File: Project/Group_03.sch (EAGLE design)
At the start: 18 parts, among them J1 POWER_JACKPTH_LOCK, U1 +12v, U3 TCA9546APW

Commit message: Add last comments + layout editing
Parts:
- added J2, J3, J4, J5: (no value), SparkFun-Connectors:CONN_02
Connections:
- net I2C_SCL_0: now also J2.2
- net I2C_SCL_1: now also J3.2
- net I2C_SCL_2: now also J4.2
- net I2C_SCL_3: now also J5.2
- net I2C_SDA_0: now also J2.1
- net I2C_SDA_1: now also J3.1
- net I2C_SDA_2: now also J4.1
- net I2C_SDA_3: now also J5.1
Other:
- note added: "4-Channel I2C"
- note added: "Analog Temeprature Sensor"
- note added: "Light Sensor"
- note added: "Power"
- note added: "The I2C expander is used to connect several BME280 sensors outside the PCB through these connectors."
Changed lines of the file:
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@@
 <part name="GND5" library="SparkFun-PowerSymbols" deviceset="GND" device=""/>
 <part name="SUPPLY7" library="SparkFun-PowerSymbols" deviceset="5V" device=""/>
+<part name="J2" library="SparkFun-Connectors" deviceset="CONN_02" device=""/>
+<part name="J3" library="SparkFun-Connectors" deviceset="CONN_02" device=""/>
+<part name="J4" library="SparkFun-Connectors" deviceset="CONN_02" device=""/>
+<part name="J5" library="SparkFun-Connectors" deviceset="CONN_02" device=""/>
 </parts>
 <sheets>
@@
 <wire x1="132.08" y1="175.26" x2="271.78" y2="175.26" width="0.1524" layer="97"/>
 <wire x1="271.78" y1="175.26" x2="271.78" y2="101.6" width="0.1524" layer="97"/>
-<wire x1="271.78" y1="101.6" x2="132.08" y2="101.6" width="0.1524" layer="97"/>
+<wire x1="271.78" y1="101.6" x2="220.98" y2="101.6" width="0.1524" layer="97"/>
+<wire x1="220.98" y1="101.6" x2="132.08" y2="101.6" width="0.1524" layer="97"/>
 <wire x1="132.08" y1="101.6" x2="132.08" y2="134.62" width="0.1524" layer="97"/>
+<wire x1="271.78" y1="22.86" x2="271.78" y2="86.36" width="0.1524" layer="97"/>
+<text x="231.14" y="88.9" size="1.778" layer="97">The I2C expander is used to
+connect several BME280
+sensors outside the PCB
+through these connectors.</text>
+<wire x1="271.78" y1="86.36" x2="271.78" y2="101.6" width="0.1524" layer="97"/>
+<wire x1="220.98" y1="101.6" x2="220.98" y2="86.36" width="0.1524" layer="97"/>
+<wire x1="220.98" y1="86.36" x2="220.98" y2="22.86" width="0.1524" layer="97"/>
+<wire x1="220.98" y1="22.86" x2="271.78" y2="22.86" width="0.1524" layer="97"/>
+<wire x1="220.98" y1="86.36" x2="271.78" y2="86.36" width="0.1524" layer="97"/>
+<text x="30.48" y="60.96" size="1.778" layer="97">Analog Temeprature
+Sensor</text>
+<text x="38.1" y="73.66" size="1.778" layer="97">Light Sensor</text>
+<text x="60.96" y="139.7" size="1.778" layer="97">Power</text>
+<text x="167.64" y="170.18" size="1.778" layer="97">4-Channel I2C</text>
 </plain>
 <instances>
@@
 <instance part="SUPPLY7" gate="G$1" x="149.86" y="162.56" smashed="yes">
 <attribute name="VALUE" x="149.86" y="165.354" size="1.778" layer="96" align="bottom-center"/>
+</instance>
+<instance part="J2" gate="G$1" x="236.22" y="76.2" smashed="yes">
+<attribute name="VALUE" x="233.68" y="71.374" size="1.778" layer="96" font="vector"/>
+<attribute name="NAME" x="233.68" y="81.788" size="1.778" layer="95" font="vector"/>
+</instance>
+<instance part="J3" gate="G$1" x="236.22" y="60.96" smashed="yes">
+<attribute name="VALUE" x="233.68" y="56.134" size="1.778" layer="96" font="vector"/>
+<attribute name="NAME" x="233.68" y="66.548" size="1.778" layer="95" font="vector"/>
+</instance>
+<instance part="J4" gate="G$1" x="236.22" y="45.72" smashed="yes">
+<attribute name="VALUE" x="233.68" y="40.894" size="1.778" layer="96" font="vector"/>
+<attribute name="NAME" x="233.68" y="51.308" size="1.778" layer="95" font="vector"/>
+</instance>
+<instance part="J5" gate="G$1" x="236.22" y="30.48" smashed="yes">
+<attribute name="VALUE" x="233.68" y="25.654" size="1.778" layer="96" font="vector"/>
+<attribute name="NAME" x="233.68" y="36.068" size="1.778" layer="95" font="vector"/>
 </instance>
 </instances>
@@
 <label x="185.42" y="147.32" size="1.778" layer="95"/>
 </segment>
+<segment>
+<pinref part="J2" gate="G$1" pin="2"/>
+<wire x1="243.84" y1="78.74" x2="254" y2="78.74" width="0.1524" layer="91"/>
+<label x="246.38" y="78.74" size="1.778" layer="95"/>
+</segment>
 </net>
 <net name="I2C_SDA_0" class="0">
@@
 <label x="185.42" y="144.78" size="1.778" layer="95"/>
 </segment>
+<segment>
+<pinref part="J2" gate="G$1" pin="1"/>
+<wire x1="243.84" y1="76.2" x2="254" y2="76.2" width="0.1524" layer="91"/>
+<label x="246.38" y="76.2" size="1.778" layer="95"/>
+</segment>
 </net>
 <net name="I2C_SCL_1" class="0">
@@
 <label x="185.42" y="137.16" size="1.778" layer="95"/>
 </segment>
+<segment>
+<pinref part="J3" gate="G$1" pin="2"/>
+<wire x1="243.84" y1="63.5" x2="254" y2="63.5" width="0.1524" layer="91"/>
+<label x="246.38" y="63.5" size="1.778" layer="95"/>
+</segment>
 </net>
 <net name="I2C_SDA_1" class="0">
@@
 <label x="185.42" y="134.62" size="1.778" layer="95"/>
 </segment>
+<segment>
+<pinref part="J3" gate="G$1" pin="1"/>
+<wire x1="243.84" y1="60.96" x2="254" y2="60.96" width="0.1524" layer="91"/>
+<label x="246.38" y="60.96" size="1.778" layer="95"/>
+</segment>
 </net>
 <net name="I2C_SCL_2" class="0">
@@
 <label x="185.42" y="127" size="1.778" layer="95"/>
 </segment>
+<segment>
+<pinref part="J4" gate="G$1" pin="2"/>
+<wire x1="243.84" y1="48.26" x2="254" y2="48.26" width="0.1524" layer="91"/>
+<label x="246.38" y="48.26" size="1.778" layer="95"/>
+</segment>
 </net>
 <net name="I2C_SDA_2" class="0">
@@
 <label x="185.42" y="124.46" size="1.778" layer="95"/>
 </segment>
+<segment>
+<pinref part="J4" gate="G$1" pin="1"/>
+<wire x1="243.84" y1="45.72" x2="254" y2="45.72" width="0.1524" layer="91"/>
+<label x="246.38" y="45.72" size="1.778" layer="95"/>
+</segment>
 </net>
 <net name="I2C_SCL_3" class="0">
@@
 <label x="185.42" y="114.3" size="1.778" layer="95"/>
 </segment>
+<segment>
+<pinref part="J5" gate="G$1" pin="2"/>
+<wire x1="243.84" y1="33.02" x2="254" y2="33.02" width="0.1524" layer="91"/>
+<label x="246.38" y="33.02" size="1.778" layer="95"/>
+</segment>
 </net>
 <net name="I2C_SDA_3" class="0">
@@
 <wire x1="264.16" y1="111.76" x2="264.16" y2="119.38" width="0.1524" layer="91"/>
 <label x="185.42" y="111.76" size="1.778" layer="95"/>
+</segment>
+<segment>
+<pinref part="J5" gate="G$1" pin="1"/>
+<wire x1="243.84" y1="30.48" x2="254" y2="30.48" width="0.1524" layer="91"/>
+<label x="246.38" y="30.48" size="1.778" layer="95"/>
 </segment>
 </net>
@@
 </schematic>
 </drawing>
+<compatibility>
+<note version="6.3" minversion="6.2.2" severity="warning">
+Since Version 6.2.2 text objects can contain more than one line,
+which will not be processed correctly with this version.
+</note>
+</compatibility>
 </eagle>

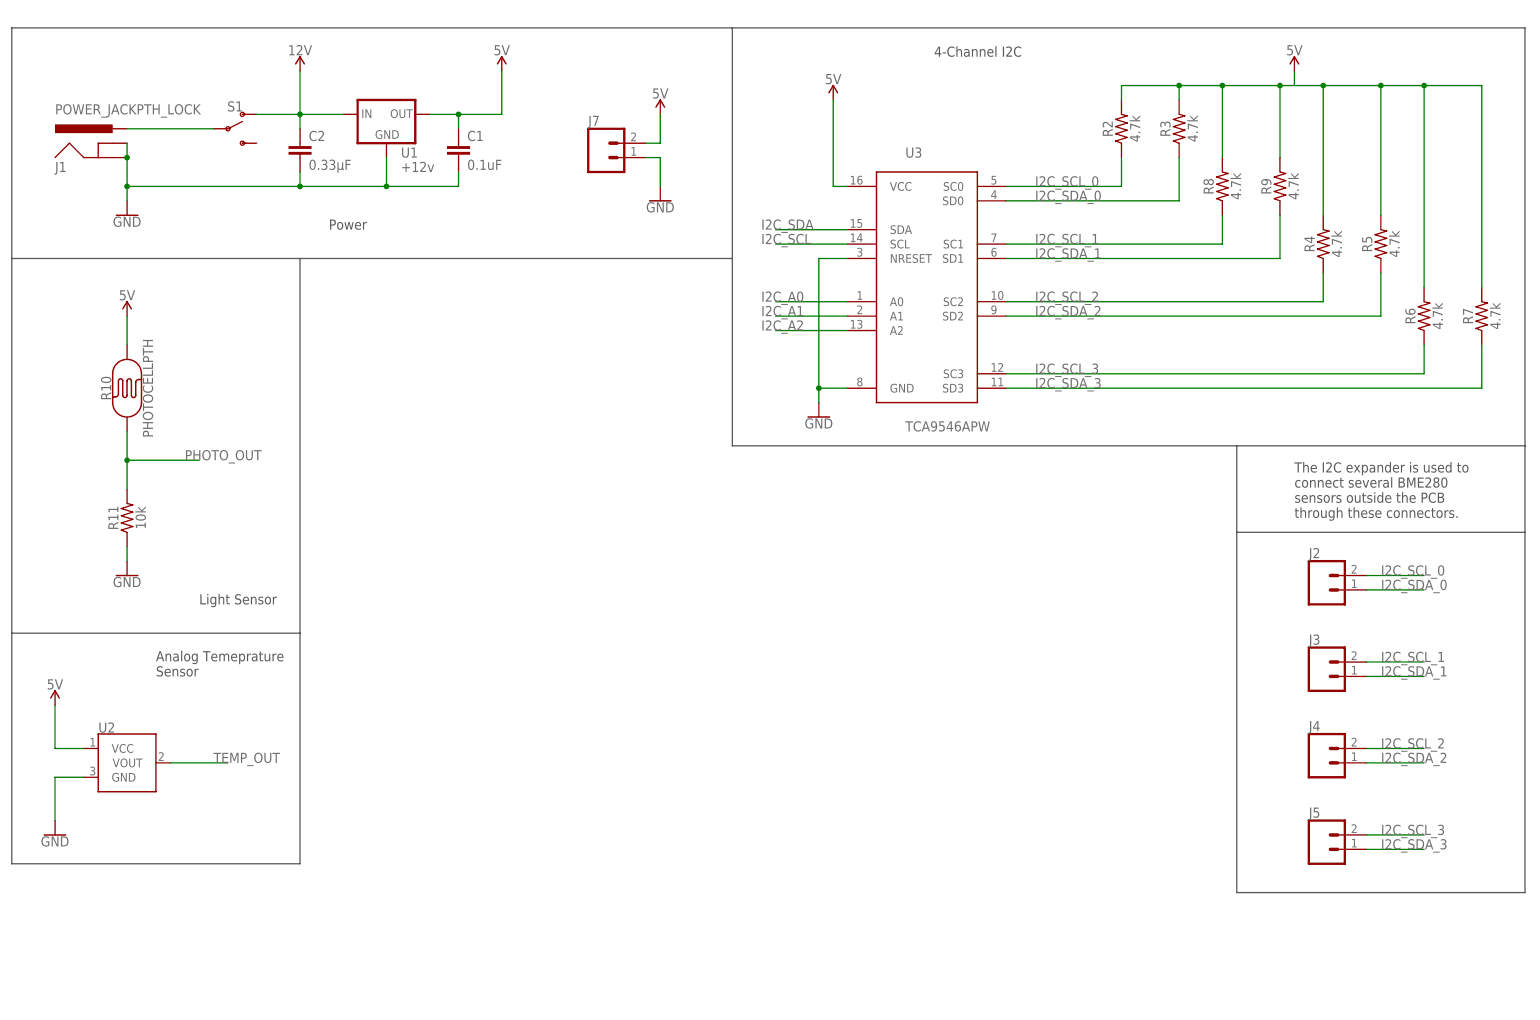
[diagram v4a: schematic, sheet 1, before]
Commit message: Add of TMUX and CY8CKIT
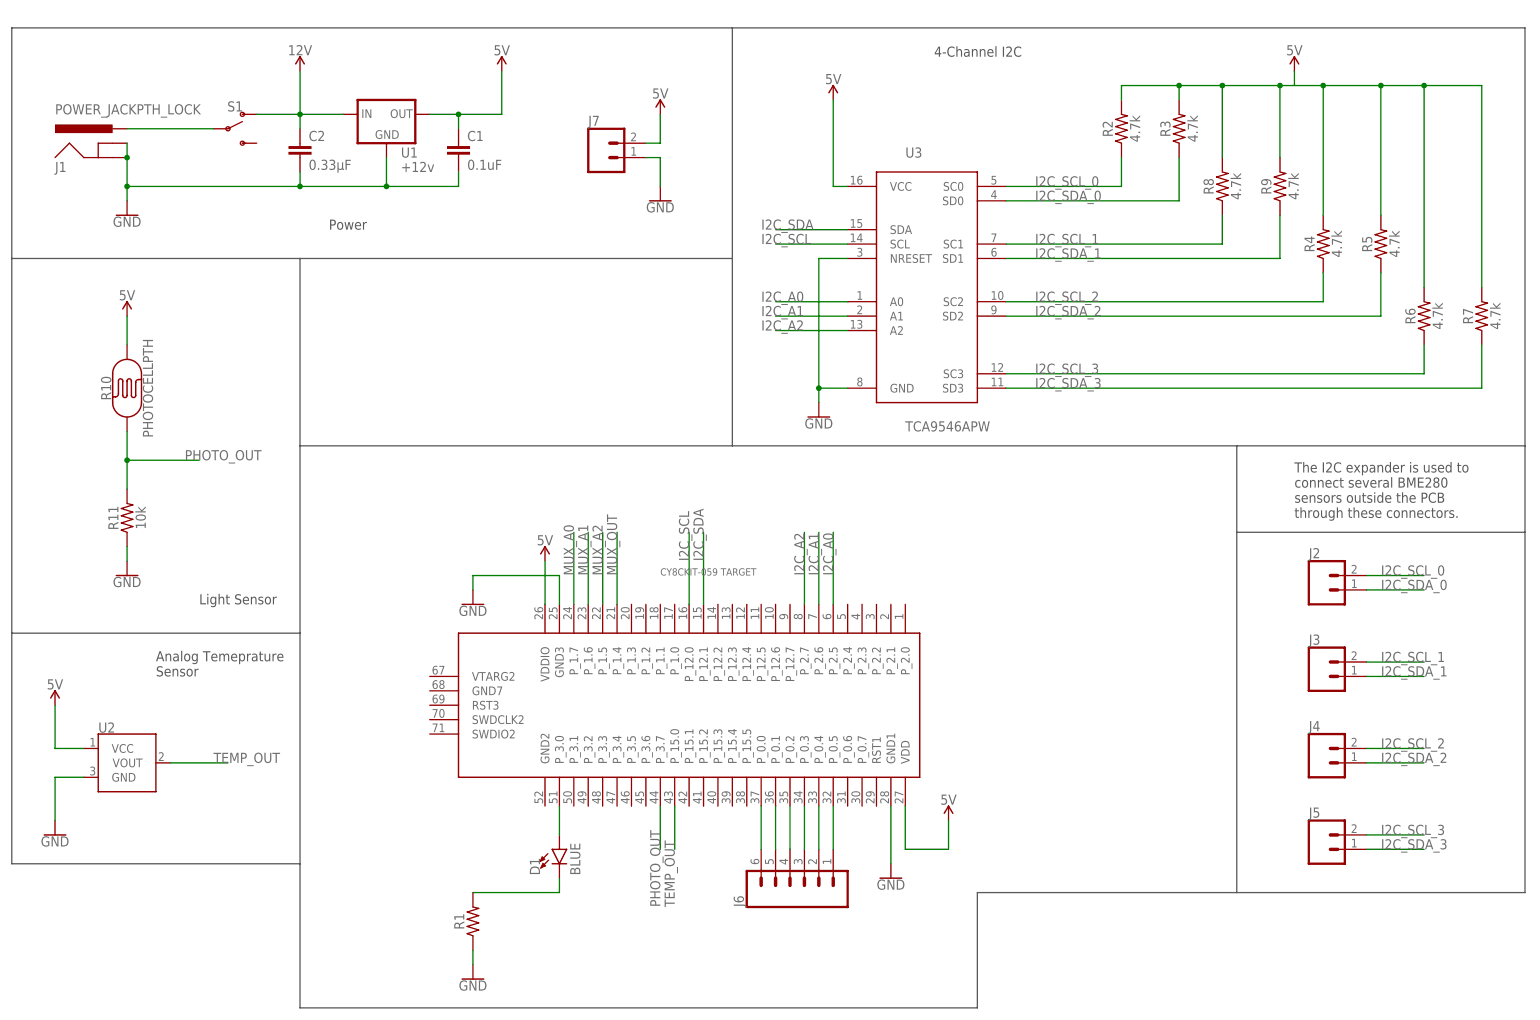
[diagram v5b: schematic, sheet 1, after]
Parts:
- added C3: 0.1uF, SparkFun-Capacitors:0.1UF-KIT-EZ-50V-20%
- added D1: BLUE, SparkFun-LED:LED-BLUE1206
- added J6: (no value), SparkFun-Connectors:CONN_06LOCK
- added J8: (no value), SparkFun-Connectors:CONN_08LOCK
- added R1: (no value), SparkFun-Resistors:RESISTORAXIAL-0.3
- added U$1: CY8CKIT-059_TARGET, CY8KIT-059:CY8CKIT-059_TARGET
- added U4: TMUX1208RSV, Group_03_Library:TMUX1208RSV
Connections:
- new net MUX_A0: U$1.P_1.7, U4.A0
- new net MUX_A1: U$1.P_1.6, U4.A1
- new net MUX_A2: U$1.P_1.5, U4.A2
- new net MUX_OUT: U$1.P_1.4, U4.D
- new net N$11: D1.C, R1.2
- new net N$12: J8.7, U4.S2
- new net N$13: J8.6, U4.S3
- new net N$14: J8.5, U4.S4
- new net N$15: J8.4, U4.S5
- new net N$16: J8.3, U4.S6
- new net N$17: J8.2, U4.S7
- new net N$18: J8.1, U4.S8
- new net N$2: J8.8, U4.S1
- new net N$3: J6.1, U$1.P_0.5
- new net N$4: J6.2, U$1.P_0.4
- new net N$5: J6.3, U$1.P_0.3
- new net N$6: J6.4, U$1.P_0.2
- new net N$7: J6.5, U$1.P_0.1
- new net N$8: J6.6, U$1.P_0.0
- new net N$9: D1.A, U$1.P_3.0
- net 5V: now also C3.1, U$1.VDD, U$1.VDDIO, U4.EN, U4.VDD
- net GND: now also C3.2, R1.1, U$1.GND1, U$1.GND3, U4.GND
- net I2C_A0: now also U$1.P_2.5
- net I2C_A1: now also U$1.P_2.6
- net I2C_A2: now also U$1.P_2.7
- net I2C_SCL: now also U$1.P_12.0
- net I2C_SDA: now also U$1.P_12.1
- net PHOTO_OUT: now also U$1.P_3.7
- net TEMP_OUT: now also U$1.P_15.0

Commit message: Completed wiring, and design rules update
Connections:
- removed net N$10: R2.2, R3.2, R4.2, R5.2, R6.2, R7.2, R8.2, R9.2
- net 5V: now also R2.2, R3.2, R4.2, R5.2, R6.2, R7.2, R8.2, R9.2

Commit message: Change silkscreen line width in Library for MUX, TCA and CY8
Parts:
- U$1: device CY8KIT-059:CY8CKIT-059_TARGET -> Group_03_Library:CY8CKIT-059_TARGET
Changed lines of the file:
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@@
 <part name="J4" library="SparkFun-Connectors" deviceset="CONN_02" device=""/>
 <part name="J5" library="SparkFun-Connectors" deviceset="CONN_02" device=""/>
-<part name="U$1" library="CY8KIT-059" deviceset="CY8CKIT-059_TARGET" device=""/>
+<part name="U$1" library="Group_03_Library" deviceset="CY8CKIT-059_TARGET" device=""/>
 <part name="J6" library="SparkFun-Connectors" deviceset="CONN_06" device="LOCK"/>
 <part name="D1" library="SparkFun-LED" deviceset="LED-BLUE" device="1206" value="BLUE"/>

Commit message: Last modifications to schematic, board and check rules
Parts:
- R1: value (none) -> 330
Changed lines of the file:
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@@
 <part name="J6" library="SparkFun-Connectors" deviceset="CONN_06" device="LOCK"/>
 <part name="D1" library="SparkFun-LED" deviceset="LED-BLUE" device="1206" value="BLUE"/>
-<part name="R1" library="SparkFun-Resistors" deviceset="RESISTOR" device="AXIAL-0.3" value=" "/>
+<part name="R1" library="SparkFun-Resistors" deviceset="RESISTOR" device="AXIAL-0.3" value=" 330"/>
 <part name="SUPPLY8" library="SparkFun-PowerSymbols" deviceset="5V" device=""/>
 <part name="SUPPLY9" library="SparkFun-PowerSymbols" deviceset="5V" device=""/>
